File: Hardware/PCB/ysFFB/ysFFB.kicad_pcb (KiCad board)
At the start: 2 copper layers, 423.6 x 175 mm, 279 parts, among them J1 Synth_power_2x5, J10 AudioJack2, J11 AudioJack2, J12 AudioJack2, J13 AudioJack2, J14 AudioJack2, J15 Conn_01x04, J16 Conn_01x03, J2 Conn_01x08, J3 Conn_01x06, J4 Conn_01x04, J5 Conn_02x07_Odd_Even, J6 Conn_01x03, J7 Conn_01x08, J8 Conn_02x07_Odd_Even, J9 Conn_01x06, U1 TL074, U2 TL074, U3 TL074, U4 TL074, U5 TL074, U6 TL074, U7 TL074, U8 TL074

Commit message: Pre fab tweaks, new Gerbers, correct alignment and make PCB dimensions symmetric in module
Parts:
- J10, J11, J12, J13, J14: footprint ao_tht:Jack_6.35mm_PJ_629HAN -> ao_tht:Jack_6.35mm_PJ_629HAN_slots
- RN1, RN2, RN3, RN4: value R_Network08 -> 100k
- moved GRAF1 1.00 mm to (-103.2, 121.0)
- moved H2 1.00 mm to (220.4, 35.0)
- moved H4 1.00 mm to (220.4, 191.0)
- moved H6 1.00 mm to (-8.20, 35.0)
- moved H8 1.00 mm to (-8.20, 191.0)
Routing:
- net /Panel components/BP10PP: track 120.6 -> 121.5 mm
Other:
- board size 423.6 x 175 mm -> 424.6 x 175 mm
- board text added: "Original design and layout by Yves Usson Adapted by Rich Holmes Aug 2021 https://github.com/holmesrichards/ffbmod"
- board text removed: "Original design and layout by Yves Usson Adapted by Rich Holmes Aug 2021"

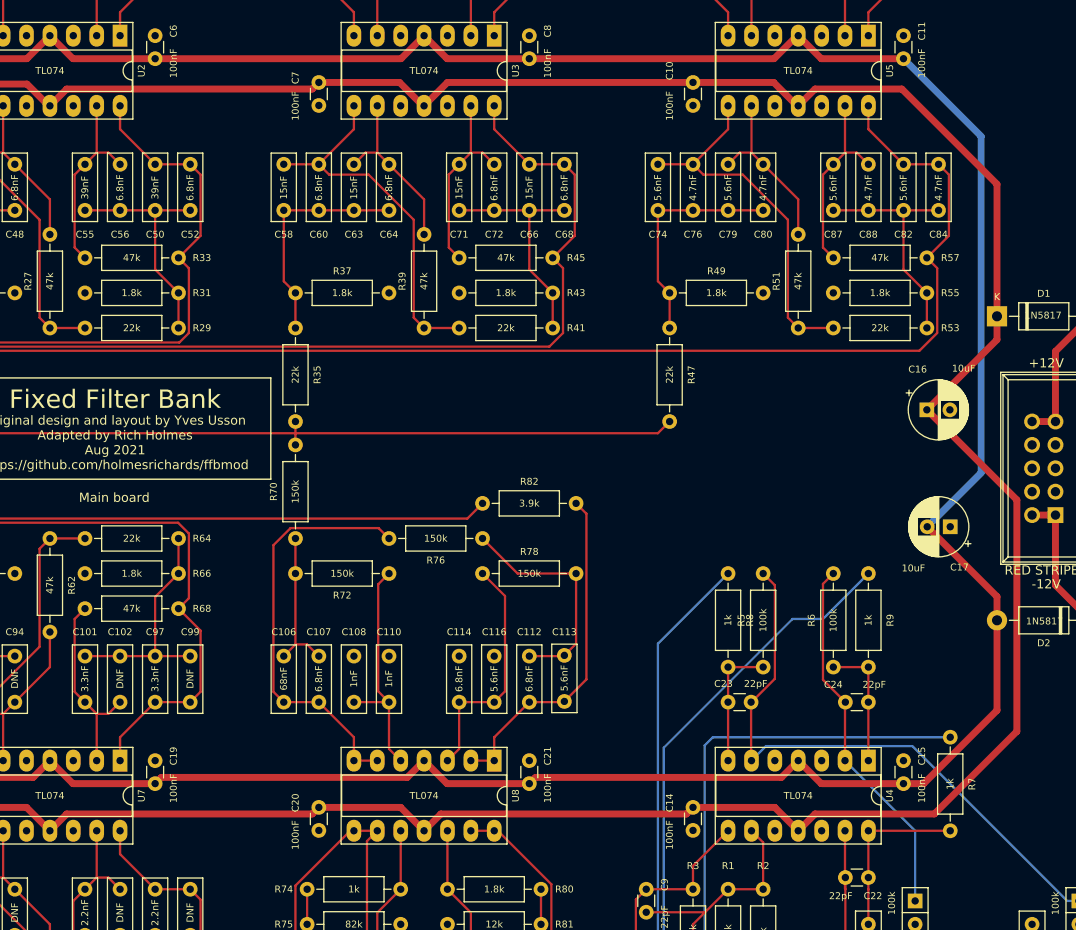
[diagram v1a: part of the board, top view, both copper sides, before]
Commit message: Fix and document power connection error
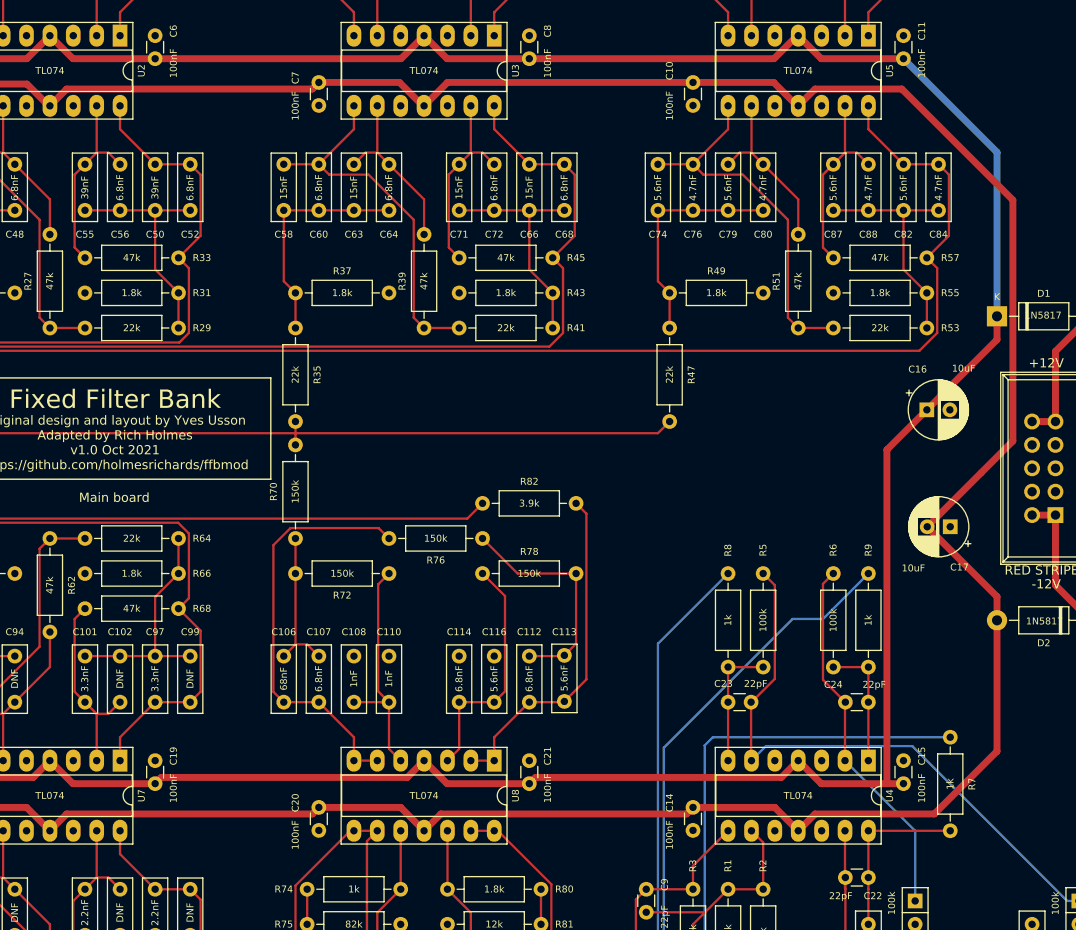
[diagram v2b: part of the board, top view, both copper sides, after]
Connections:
- C1 pad 1: +12V -> -12V
- C10 pad 1: +12V -> -12V
- C11 pad 2: -12V -> +12V
- C12 pad 1: +12V -> -12V
- C13 pad 2: -12V -> +12V
- C14 pad 1: +12V -> -12V
- C15 pad 2: -12V -> +12V
- C18 pad 1: +12V -> -12V
- C19 pad 2: -12V -> +12V
- C2 pad 2: -12V -> +12V
- C20 pad 1: +12V -> -12V
- C21 pad 2: -12V -> +12V
- C5 pad 1: +12V -> -12V
- C6 pad 2: -12V -> +12V
- C7 pad 1: +12V -> -12V
- C8 pad 2: -12V -> +12V
- U1 pad 11: +12V -> -12V
- U1 pad 4: -12V -> +12V
- U2 pad 11: +12V -> -12V
- U2 pad 4: -12V -> +12V
- U3 pad 11: +12V -> -12V
- U3 pad 4: -12V -> +12V
- U4 pad 11: +12V -> -12V
- U4 pad 4: -12V -> +12V
- U5 pad 11: +12V -> -12V
- U5 pad 4: -12V -> +12V
- U6 pad 11: +12V -> -12V
- U6 pad 4: -12V -> +12V
- U7 pad 11: +12V -> -12V
- U7 pad 4: -12V -> +12V
- U8 pad 11: +12V -> -12V
- U8 pad 4: -12V -> +12V
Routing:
- net +12V: track 402.8 -> 369.1 mm
- net -12V: track 374.5 -> 402.4 mm
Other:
- board text added: "Original design and layout by Yves Usson Adapted by Rich Holmes v1.0 Oct 2021 https://github.com/holmesrichards/ffbmod"
- board text removed: "Original design and layout by Yves Usson Adapted by Rich Holmes Aug 2021 https://github.com/holmesrichards/ffbmod"
